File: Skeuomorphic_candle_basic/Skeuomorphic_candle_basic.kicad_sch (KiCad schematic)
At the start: 14 parts, among them J2 Conn_01x02_Pin, Q1 SI2302, U1 ETA1061V33S2G

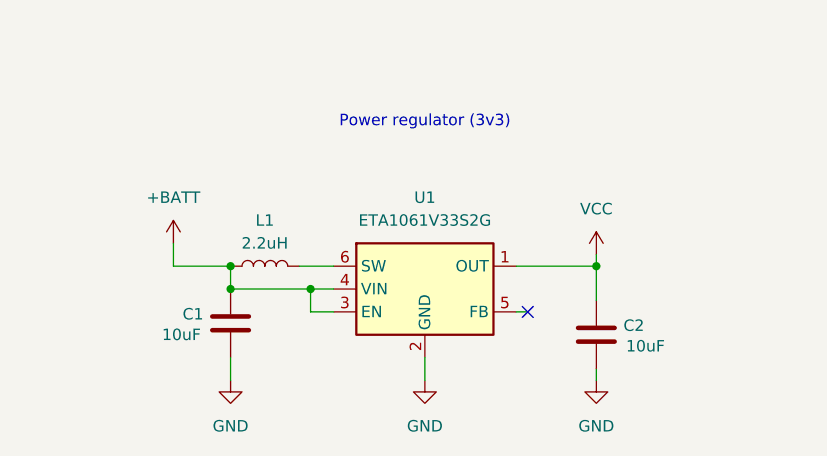
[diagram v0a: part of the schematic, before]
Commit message: added readme per pcb variant. fixed some component values
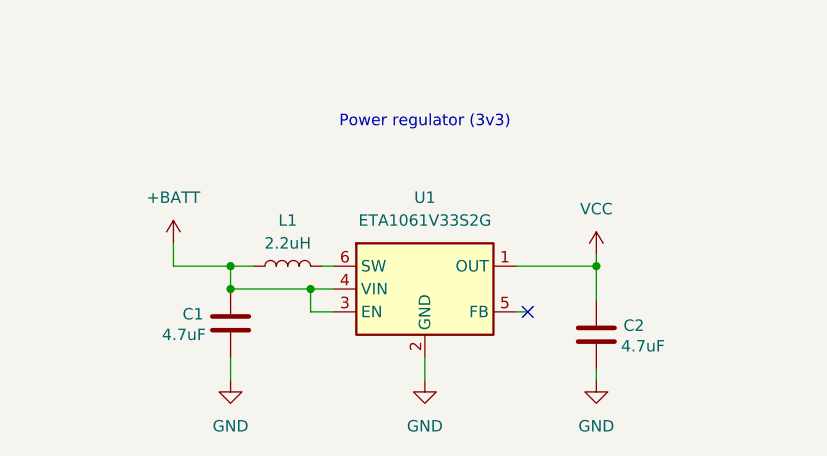
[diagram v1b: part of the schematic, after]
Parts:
- C1, C2: value 10uF -> 4.7uF
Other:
- moved on the sheet: L1
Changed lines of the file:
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@@
+	(wire
+		(pts
+			(xy 93.98 152.4) (xy 91.44 152.4)
+		)
+		(stroke
+			(width 0)
+			(type default)
+		)
+	)
 	(wire
 		(pts
@@
 	(wire
 		(pts
-			(xy 99.06 152.4) (xy 102.87 152.4)
+			(xy 101.6 152.4) (xy 102.87 152.4)
 		)
 		(stroke
@@
 	(symbol
 		(lib_id "Device:L")
-		(at 95.25 152.4 90)
+		(at 97.79 152.4 90)
 		(unit 1)
 		(body_style 1)
@@
 		(fields_autoplaced yes)
 		(property "Reference" "L1"
-			(at 95.25 147.32 90)
+			(at 97.79 147.32 90)
 			(show_name no)
 			(do_not_autoplace no)
@@
 		)
 		(property "Value" "2.2uH"
-			(at 95.25 149.86 90)
+			(at 97.79 149.86 90)
 			(show_name no)
 			(do_not_autoplace no)
@@
 		)
 		(property "Footprint" "Inductor_SMD:L_1008_2520Metric_Pad1.43x2.20mm_HandSolder"
-			(at 95.25 152.4 0)
+			(at 97.79 152.4 0)
 			(hide yes)
 			(show_name no)
@@
 		)
 		(property "Datasheet" "https://www.lcsc.com/datasheet/C964122.pdf"
-			(at 95.25 152.4 0)
+			(at 97.79 152.4 0)
 			(hide yes)
 			(show_name no)
@@
 		)
 		(property "Description" "Inductor"
-			(at 95.25 152.4 0)
+			(at 97.79 152.4 0)
 			(hide yes)
 			(show_name no)
@@
 		)
 		(property "MPN" "WIP252012P-2R2ML"
-			(at 95.25 152.4 90)
+			(at 97.79 152.4 90)
 			(hide yes)
 			(show_name no)
@@
 			)
 		)
-		(property "Value" "10uF"
+		(property "Value" "4.7uF"
 			(at 139.7 161.29 0)
 			(show_name no)
@@
 			)
 		)
-		(property "Value" "10uF"
+		(property "Value" "4.7uF"
 			(at 83.82 160.02 0)
 			(show_name no)
